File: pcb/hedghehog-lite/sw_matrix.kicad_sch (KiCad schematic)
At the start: 8 parts, among them K00 1u, K01 1u, K10 1u, K11 1u

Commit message: More edits to the schematic building v1
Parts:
- added D12, D13, D14, D15, D16, D17, D18, D2, D3, D4, D5, D6, D7, D70, D8, D81: 1N4148, Diode_SMD:D_0805_2012Metric, symbol Diode:1N4148
- added D20, D21, D22, D23, D24, D25, D26, D27, D30, D31, D32, D33, D34, D35, D36, D38, D40, D41, D42, D43, D44, D45, D46, D50, D51, D52, D53, D54, D60, D61, D62, D63, D64, D71, D72, D73, D74, D82, D83, D84, D88: 1N4148, Diode_THT:D_DO-35_SOD27_P7.62mm_Horizontal, symbol Diode:1N4148
- added K12, K13, K14, K15, K16, K17, K2, K20, K21, K22, K23, K24, K25, K26, K3, K30, K31, K32, K33, K34, K35, K38, K4, K40, K44, K45, K46, K5, K50, K51, K52, K53, K54, K6, K60, K61, K62, K63, K64, K7, K70, K71, K72, K73, K74, K81, K82, K83, K84, K88: 1u, acheron:MX100H, symbol Switch:SW_SPST
- added K18: 1.5u, acheron:MX150H, symbol Switch:SW_SPST
- added K27: 2.25u, acheron:MX225H, symbol Switch:SW_SPST
- added K36: 2.75u, acheron:MX275H, symbol Switch:SW_SPST
- added K41, K42: 1.25u, acheron:MX125H, symbol Switch:SW_SPST
- added K43: 2.75u, acheron:MX275HR, symbol Switch:SW_SPST
- added K8: 2u, acheron:MX200H, symbol Switch:SW_SPST
- D0: renamed from D1; footprint Diode_THT:D_DO-35_SOD27_P7.62mm_Horizontal -> Diode_SMD:D_SOD-123F
- D1: renamed from D3; footprint Diode_THT:D_DO-35_SOD27_P7.62mm_Horizontal -> Diode_SMD:D_0805_2012Metric
- D10: renamed from D2; footprint Diode_THT:D_DO-35_SOD27_P7.62mm_Horizontal -> Diode_SMD:D_0805_2012Metric
- D11: renamed from D4; footprint Diode_THT:D_DO-35_SOD27_P7.62mm_Horizontal -> Diode_SMD:D_0805_2012Metric
- renumbered K00 to K0, K01 to K1
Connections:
- net COL0: now also K20.1 (A), K30.1 (A), K40.1 (A), K50.1 (A), K60.1 (A), K70.1 (A)
- net COL1: now also K21.1 (A), K31.1 (A), K41.1 (A), K51.1 (A), K61.1 (A), K71.1 (A), K81.1 (A)
- net ROW0: now also D2.1 (K), D3.1 (K), D4.1 (K), D5.1 (K), D6.1 (K), D7.1 (K), D8.1 (K)
- net ROW1: now also D12.1 (K), D13.1 (K), D14.1 (K), D15.1 (K), D16.1 (K), D17.1 (K), D18.1 (K)
- new net: D16.2 (A), K16.2 (B)
- new net: D72.2 (A), K72.2 (B)
- new net: D26.2 (A), K26.2 (B)
- new net: D31.2 (A), K31.2 (B)
- new net: D4.2 (A), K4.2 (B)
- new net: D64.2 (A), K64.2 (B)
- new net: D34.2 (A), K34.2 (B)
- new net: D61.2 (A), K61.2 (B)
- new net: D46.2 (A), K46.2 (B)
- new net: D2.2 (A), K2.2 (B)
- new net: D35.2 (A), K35.2 (B)
- new net: D70.2 (A), K70.2 (B)
- new net: D6.2 (A), K6.2 (B)
- new net: D15.2 (A), K15.2 (B)
- new net: D73.2 (A), K73.2 (B)
- new net: D74.2 (A), K74.2 (B)
- new net: D27.2 (A), K27.2 (B)
- new net: D45.2 (A), K45.2 (B)
- new net: D84.2 (A), K84.2 (B)
- new net: D52.2 (A), K52.2 (B)
- new net: D14.2 (A), K14.2 (B)
- new net: D32.2 (A), K32.2 (B)
- new net: D5.2 (A), K5.2 (B)
- new net: D40.2 (A), K40.2 (B)
- new net: D33.2 (A), K33.2 (B)
- new net: D18.2 (A), K18.2 (B)
- new net: D82.2 (A), K82.2 (B)
- new net: D8.2 (A), K8.2 (B)
- new net: D88.2 (A), K88.2 (B)
- new net: D21.2 (A), K21.2 (B)
- new net: D41.2 (A), K41.2 (B)
- new net: D30.2 (A), K30.2 (B)
- new net: D53.2 (A), K53.2 (B)
- new net: D36.2 (A), K36.2 (B)
- new net: D13.2 (A), K13.2 (B)
- new net: D3.2 (A), K3.2 (B)
- new net: D38.2 (A), K38.2 (B)
- new net: D50.2 (A), K50.2 (B)
- new net: D12.2 (A), K12.2 (B)
- new net: D42.2 (A), K42.2 (B)
- new net: D20.2 (A), K20.2 (B)
- new net: D7.2 (A), K7.2 (B)
- new net: D63.2 (A), K63.2 (B)
- new net: D54.2 (A), K54.2 (B)
- new net: D83.2 (A), K83.2 (B)
- new net: D23.2 (A), K23.2 (B)
- new net: D43.2 (A), K43.2 (B)
- new net: D51.2 (A), K51.2 (B)
- new net: D22.2 (A), K22.2 (B)
- new net: D60.2 (A), K60.2 (B)
- new net: D81.2 (A), K81.2 (B)
- new net: D17.2 (A), K17.2 (B)
- new net: D71.2 (A), K71.2 (B)
- new net: D25.2 (A), K25.2 (B)
- new net: D62.2 (A), K62.2 (B)
- new net: D24.2 (A), K24.2 (B)
- new net: D44.2 (A), K44.2 (B)
- new net COL2: K12.1 (A), K2.1 (A), K22.1 (A), K32.1 (A), K42.1 (A), K52.1 (A), K62.1 (A), K72.1 (A), K82.1 (A)
- new net COL3: K13.1 (A), K23.1 (A), K3.1 (A), K33.1 (A), K43.1 (A), K53.1 (A), K63.1 (A), K73.1 (A), K83.1 (A)
- new net COL4: K14.1 (A), K24.1 (A), K34.1 (A), K4.1 (A), K44.1 (A), K54.1 (A), K64.1 (A), K74.1 (A), K84.1 (A)
- new net COL5: K15.1 (A), K25.1 (A), K35.1 (A), K45.1 (A), K5.1 (A)
- new net COL6: K16.1 (A), K26.1 (A), K36.1 (A), K46.1 (A), K6.1 (A)
- new net COL7: K17.1 (A), K27.1 (A), K7.1 (A)
- new net COL8: K18.1 (A), K38.1 (A), K8.1 (A), K88.1 (A)
- new net ROW2: D20.1 (K), D21.1 (K), D22.1 (K), D23.1 (K), D24.1 (K), D25.1 (K), D26.1 (K), D27.1 (K)
- new net ROW3: D30.1 (K), D31.1 (K), D32.1 (K), D33.1 (K), D34.1 (K), D35.1 (K), D36.1 (K), D38.1 (K)
- new net ROW4: D40.1 (K), D41.1 (K), D42.1 (K), D43.1 (K), D44.1 (K), D45.1 (K), D46.1 (K)
- new net ROW5: D50.1 (K), D51.1 (K), D52.1 (K), D53.1 (K), D54.1 (K)
- new net ROW6: D60.1 (K), D61.1 (K), D62.1 (K), D63.1 (K), D64.1 (K)
- new net ROW7: D70.1 (K), D71.1 (K), D72.1 (K), D73.1 (K), D74.1 (K)
- new net ROW8: D81.1 (K), D82.1 (K), D83.1 (K), D84.1 (K), D88.1 (K)
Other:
- moved on the sheet: D0, D1, D10, D11, K0, K1, K10, K11

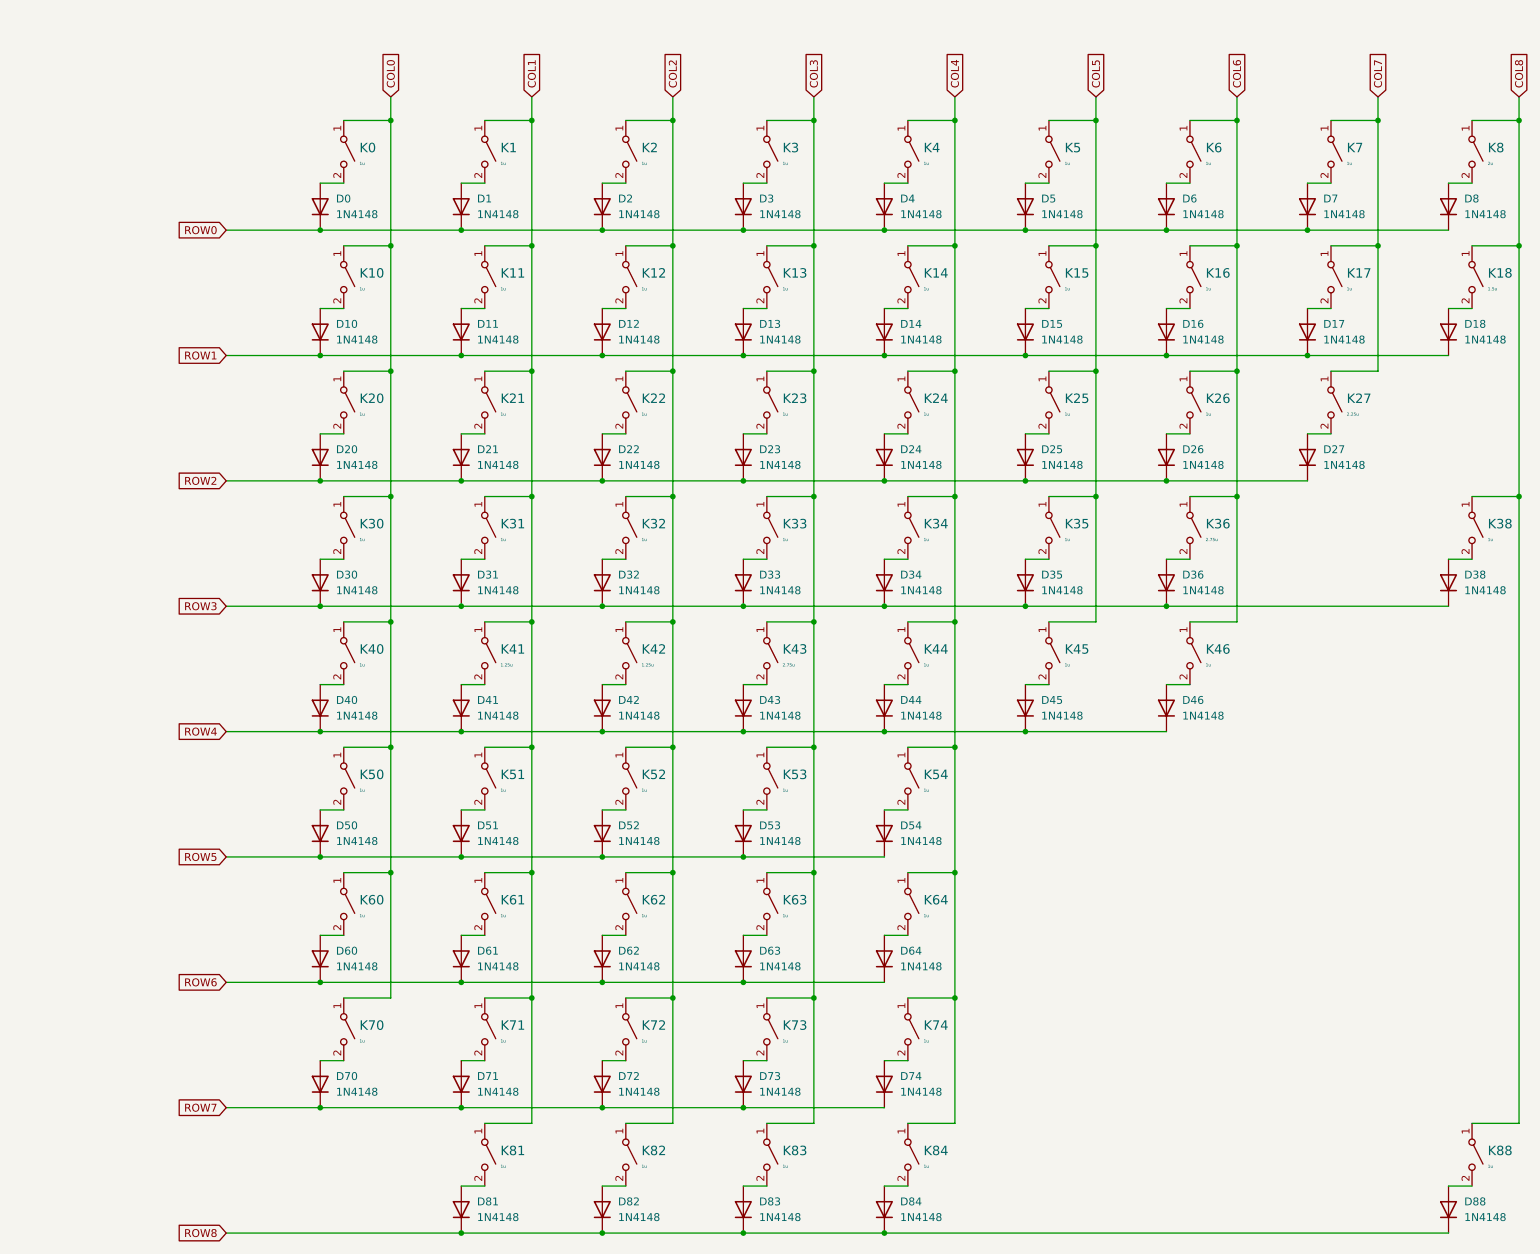
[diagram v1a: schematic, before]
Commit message: Placed all components on PCB
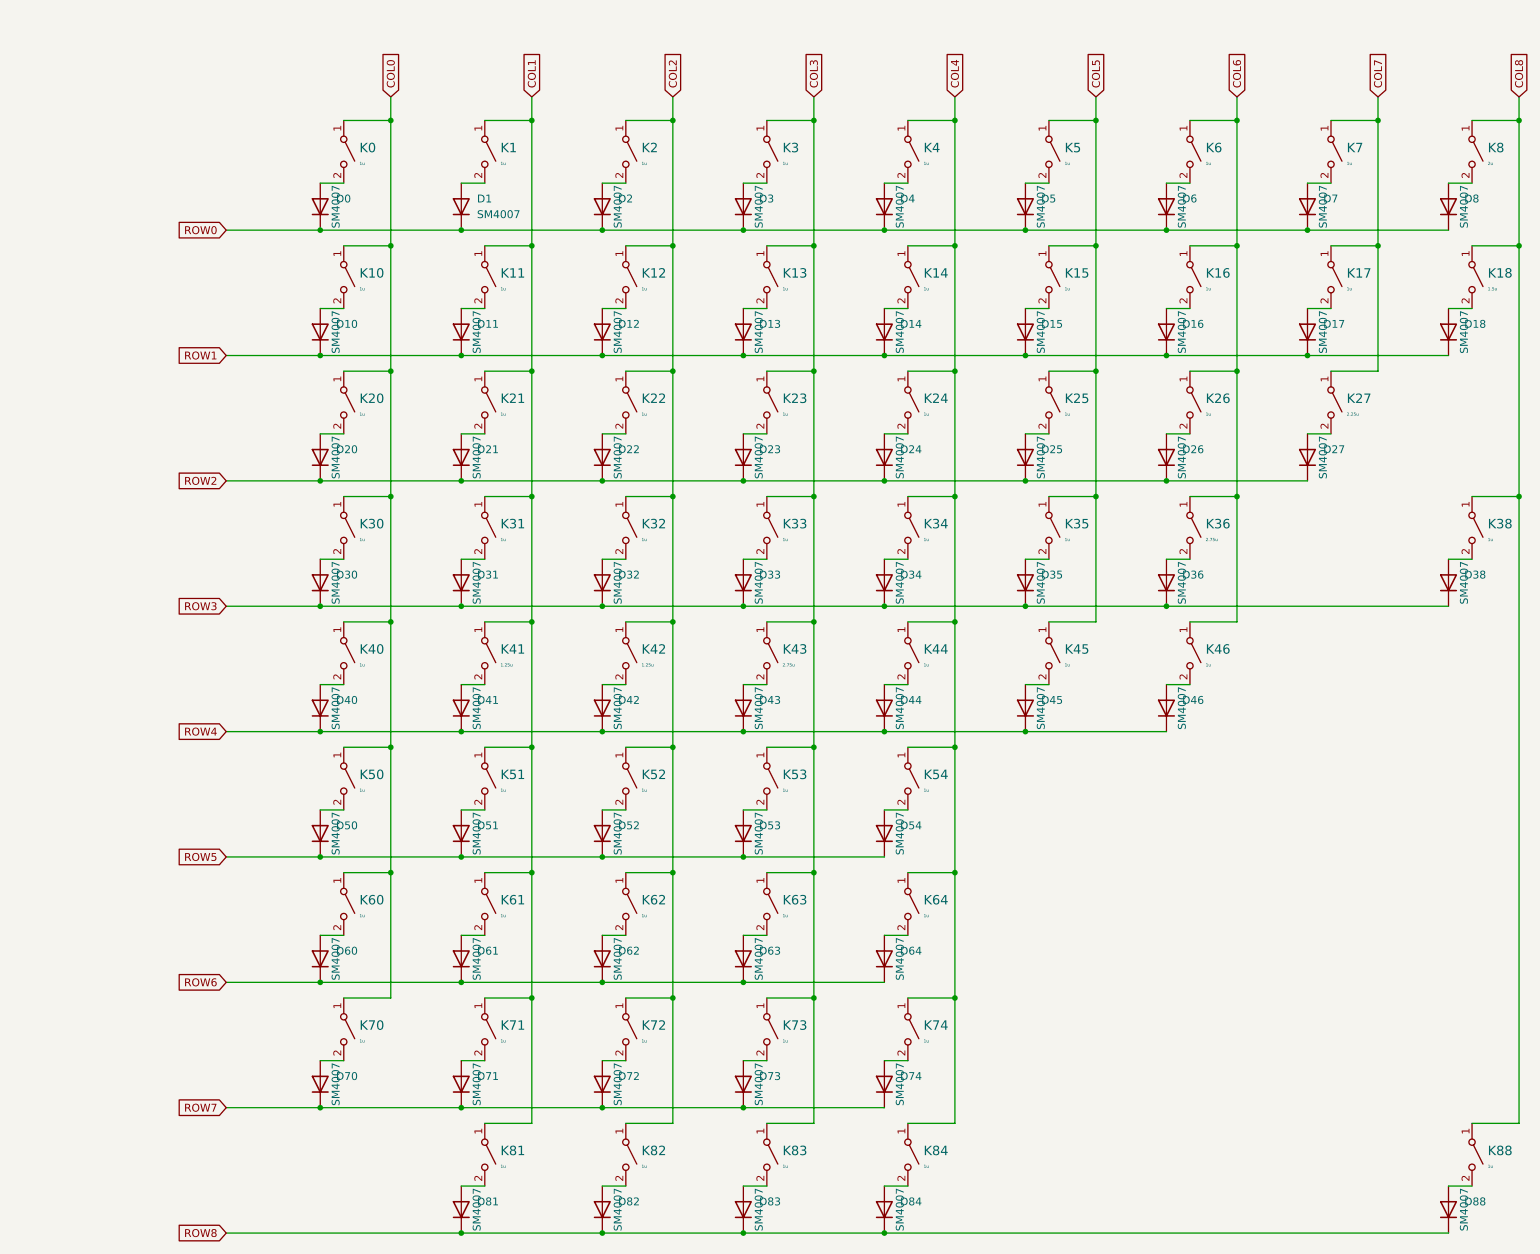
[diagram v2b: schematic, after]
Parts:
- D0: value 1N4148 -> SM4007; symbol Diode:1N4148 -> Diode:SM4007; LCSC Part # (none) -> C64898
- D1, D10, D11, D12, D13, D14, D15, D16, D17, D18, D2, D3, D4, D5, D6, D7, D70, D8, D81: value 1N4148 -> SM4007; footprint Diode_SMD:D_0805_2012Metric -> Diode_SMD:D_SOD-123F; symbol Diode:1N4148 -> Diode:SM4007; LCSC Part # (none) -> C64898
- D20, D21, D22, D23, D24, D25, D26, D27, D30, D31, D32, D33, D34, D35, D36, D38, D40, D41, D42, D43, D44, D45, D46, D50, D51, D52, D53, D54, D60, D61, D62, D63, D64, D71, D72, D73, D74, D82, D83, D84, D88: value 1N4148 -> SM4007; footprint Diode_THT:D_DO-35_SOD27_P7.62mm_Horizontal -> Diode_SMD:D_SOD-123F; symbol Diode:1N4148 -> Diode:SM4007; LCSC Part # (none) -> C64898
- K0, K1, K10, K11, K12, K13, K14, K15, K16, K17, K18, K2, K20, K21, K22, K23, K24, K25, K26, K27, K3, K30, K31, K32, K33, K34, K35, K36, K38, K4, K40, K41, K42, K43, K44, K45, K46, K5, K50, K51, K52, K53, K54, K6, K60, K61, K62, K63, K64, K7, K70, K71, K72, K73, K74, K8, K81, K82, K83, K84, K88: LCSC Part # (none) -> C2803348

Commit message: Initial fabrication files and update to Kailh socket parts
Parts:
- K0, K1, K10, K11, K12, K13, K14, K15, K16, K17, K18, K2, K20, K21, K22, K23, K24, K25, K26, K27, K3, K30, K31, K32, K33, K34, K35, K36, K38, K4, K40, K41, K42, K43, K44, K45, K46, K5, K50, K51, K52, K53, K54, K6, K60, K61, K62, K63, K64, K7, K70, K71, K72, K73, K74, K8, K81, K82, K83, K84, K88: LCSC Part # C2803348 -> C5156480
